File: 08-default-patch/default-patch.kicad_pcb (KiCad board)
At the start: 2 copper layers, 210.7 x 32.5 mm, 30 parts

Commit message: Reverted default patch
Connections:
- J_MIXER1 pad 5: Net-(JP6-B) -> Net-(JP4-B)
- J_MIXER1 pad 6: Net-(JP6-B) -> Net-(JP4-B)
- J_MIXER1 pad 7: Net-(JP4-B) -> Net-(JP6-B)
- J_MIXER1 pad 8: Net-(JP4-B) -> Net-(JP6-B)
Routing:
- net Net-(JP4-B): track 100.9 -> 98.8 mm
- net Net-(JP6-B): track 42.5 -> 44.4 mm
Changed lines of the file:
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@@
 			(layers "*.Cu" "*.Mask")
 			(remove_unused_layers no)
-			(net 29 "Net-(JP6-B)")
+			(net 26 "Net-(JP4-B)")
 			(pinfunction "Pin_5")
 			(pintype "passive")
@@
 			(layers "*.Cu" "*.Mask")
 			(remove_unused_layers no)
-			(net 29 "Net-(JP6-B)")
+			(net 26 "Net-(JP4-B)")
 			(pinfunction "Pin_6")
 			(pintype "passive")
@@
 			(layers "*.Cu" "*.Mask")
 			(remove_unused_layers no)
-			(net 26 "Net-(JP4-B)")
+			(net 29 "Net-(JP6-B)")
 			(pinfunction "Pin_7")
 			(pintype "passive")
@@
 			(layers "*.Cu" "*.Mask")
 			(remove_unused_layers no)
-			(net 26 "Net-(JP4-B)")
+			(net 29 "Net-(JP6-B)")
 			(pinfunction "Pin_8")
 			(pintype "passive")
@@
 	)
 	(segment
-		(start 198.62 67.049)
-		(end 198.62 65.54)
+		(start 196.08 65.54)
+		(end 196.08 63)
 		(width 0.508)
 		(layer "F.Cu")
@@
 	)
 	(segment
-		(start 198.62 63)
-		(end 198.62 65.54)
+		(start 195.128 68.763)
+		(end 196.08 67.811)
 		(width 0.508)
 		(layer "F.Cu")
@@
 	)
 	(segment
-		(start 196.906 68.763)
-		(end 198.62 67.049)
+		(start 196.08 67.811)
+		(end 196.08 65.54)
 		(width 0.508)
 		(layer "F.Cu")
@@
 	(segment
 		(start 144.963 68.763)
-		(end 196.906 68.763)
+		(end 195.128 68.763)
 		(width 0.508)
 		(layer "F.Cu")
@@
 	)
 	(segment
-		(start 196.08 65.54)
-		(end 196.08 63)
-		(width 0.508)
-		(layer "F.Cu")
-		(net 29)
-	)
-	(segment
-		(start 196.08 69.208)
-		(end 196.08 65.54)
+		(start 198.62 68.065)
+		(end 198.62 63)
 		(width 0.508)
 		(layer "B.Cu")
@@
 	)
 	(segment
-		(start 160.091 69.906)
-		(end 195.382 69.906)
+		(start 196.779 69.906)
+		(end 198.62 68.065)
 		(width 0.508)
 		(layer "B.Cu")
@@
 	)
 	(segment
-		(start 195.382 69.906)
-		(end 196.08 69.208)
+		(start 160.091 69.906)
+		(end 196.779 69.906)
 		(width 0.508)
 		(layer "B.Cu")

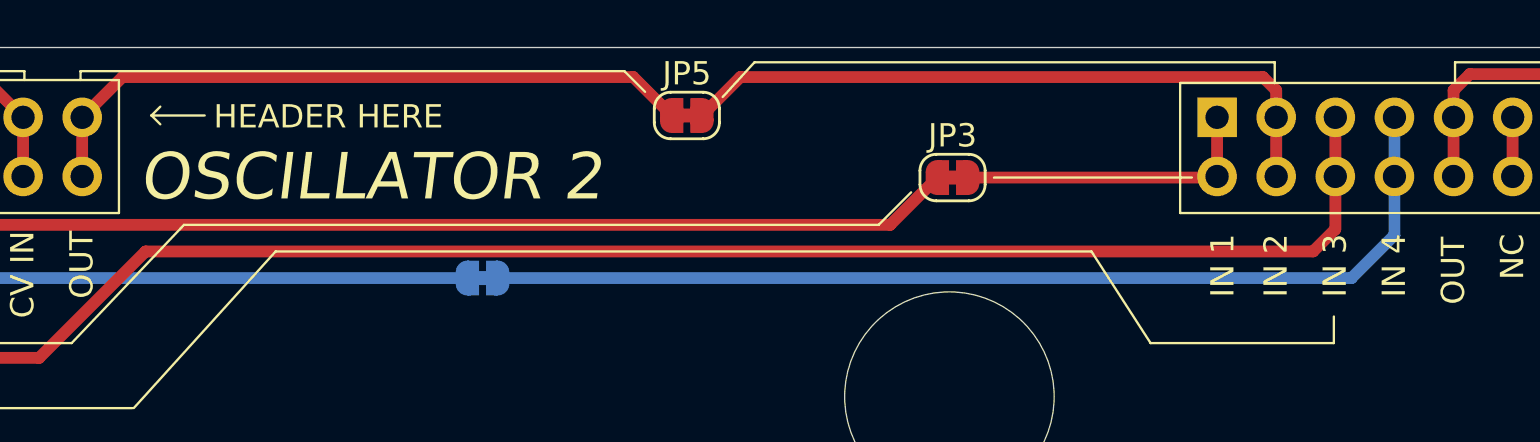
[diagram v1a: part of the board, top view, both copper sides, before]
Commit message: Updated default patch for noise <> SUB
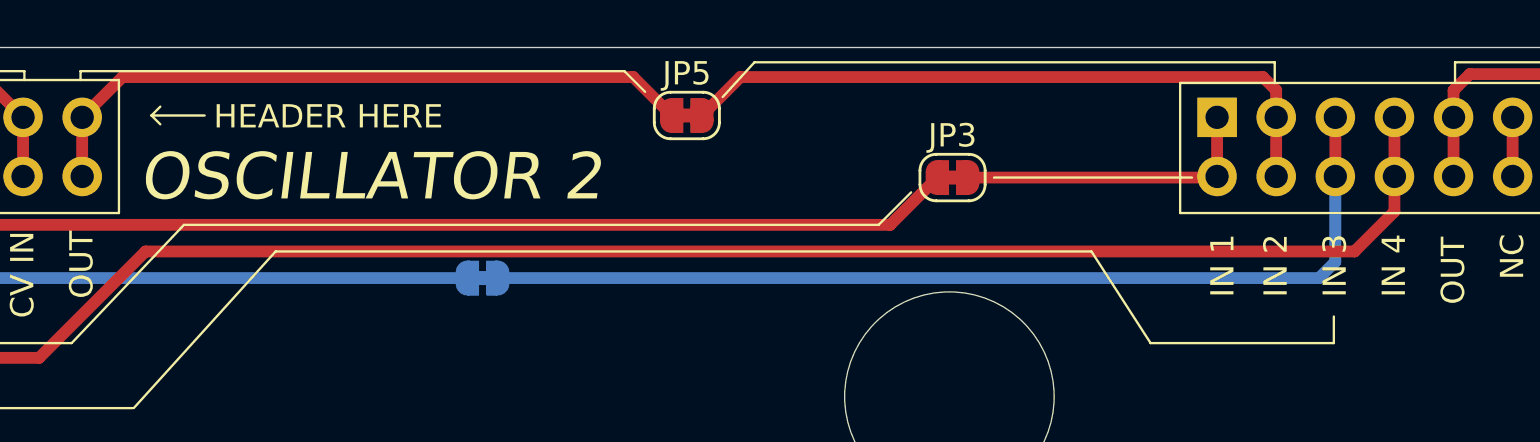
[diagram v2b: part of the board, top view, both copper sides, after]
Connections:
- J_MIXER1 pad 5: Net-(JP4-B) -> Net-(JP6-B)
- J_MIXER1 pad 6: Net-(JP4-B) -> Net-(JP6-B)
- J_MIXER1 pad 7: Net-(JP6-B) -> Net-(JP4-B)
- J_MIXER1 pad 8: Net-(JP6-B) -> Net-(JP4-B)
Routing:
- net Net-(JP4-B): track 98.8 -> 100.9 mm
- net Net-(JP6-B): track 44.4 -> 42.5 mm
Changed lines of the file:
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@@
 			(layers "*.Cu" "*.Mask")
 			(remove_unused_layers no)
-			(net 26 "Net-(JP4-B)")
+			(net 29 "Net-(JP6-B)")
 			(pinfunction "Pin_5")
 			(pintype "passive")
@@
 			(layers "*.Cu" "*.Mask")
 			(remove_unused_layers no)
-			(net 26 "Net-(JP4-B)")
+			(net 29 "Net-(JP6-B)")
 			(pinfunction "Pin_6")
 			(pintype "passive")
@@
 			(layers "*.Cu" "*.Mask")
 			(remove_unused_layers no)
-			(net 29 "Net-(JP6-B)")
+			(net 26 "Net-(JP4-B)")
 			(pinfunction "Pin_7")
 			(pintype "passive")
@@
 			(layers "*.Cu" "*.Mask")
 			(remove_unused_layers no)
-			(net 29 "Net-(JP6-B)")
+			(net 26 "Net-(JP4-B)")
 			(pinfunction "Pin_8")
 			(pintype "passive")
@@
 	)
 	(segment
-		(start 196.08 65.54)
-		(end 196.08 63)
+		(start 198.62 67.049)
+		(end 198.62 65.54)
 		(width 0.508)
 		(layer "F.Cu")
@@
 	)
 	(segment
-		(start 195.128 68.763)
-		(end 196.08 67.811)
+		(start 198.62 63)
+		(end 198.62 65.54)
 		(width 0.508)
 		(layer "F.Cu")
@@
 	)
 	(segment
-		(start 196.08 67.811)
-		(end 196.08 65.54)
+		(start 196.906 68.763)
+		(end 198.62 67.049)
 		(width 0.508)
 		(layer "F.Cu")
@@
 	(segment
 		(start 144.963 68.763)
-		(end 195.128 68.763)
+		(end 196.906 68.763)
 		(width 0.508)
 		(layer "F.Cu")
@@
 	)
 	(segment
-		(start 198.62 68.065)
-		(end 198.62 63)
+		(start 196.08 65.54)
+		(end 196.08 63)
 		(width 0.508)
-		(layer "B.Cu")
+		(layer "F.Cu")
 		(net 29)
 	)
 	(segment
-		(start 196.779 69.906)
-		(end 198.62 68.065)
+		(start 196.08 69.208)
+		(end 196.08 65.54)
 		(width 0.508)
 		(layer "B.Cu")
@@
 	(segment
 		(start 160.091 69.906)
-		(end 196.779 69.906)
+		(end 195.382 69.906)
+		(width 0.508)
+		(layer "B.Cu")
+		(net 29)
+	)
+	(segment
+		(start 195.382 69.906)
+		(end 196.08 69.208)
 		(width 0.508)
 		(layer "B.Cu")
